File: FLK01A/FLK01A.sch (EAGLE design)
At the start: 31 parts, among them J1 M10SMD_MALE, J2 M10SMD_MALE, U1 LPC812TSSOP20, U2 EKMBTO5, U3 HTU21DSMD, U4 MMA8452Q, U5 VCNL4000, U6 MPL3115A2LGA8, U7 MMDT3904, Y1 12MHZ

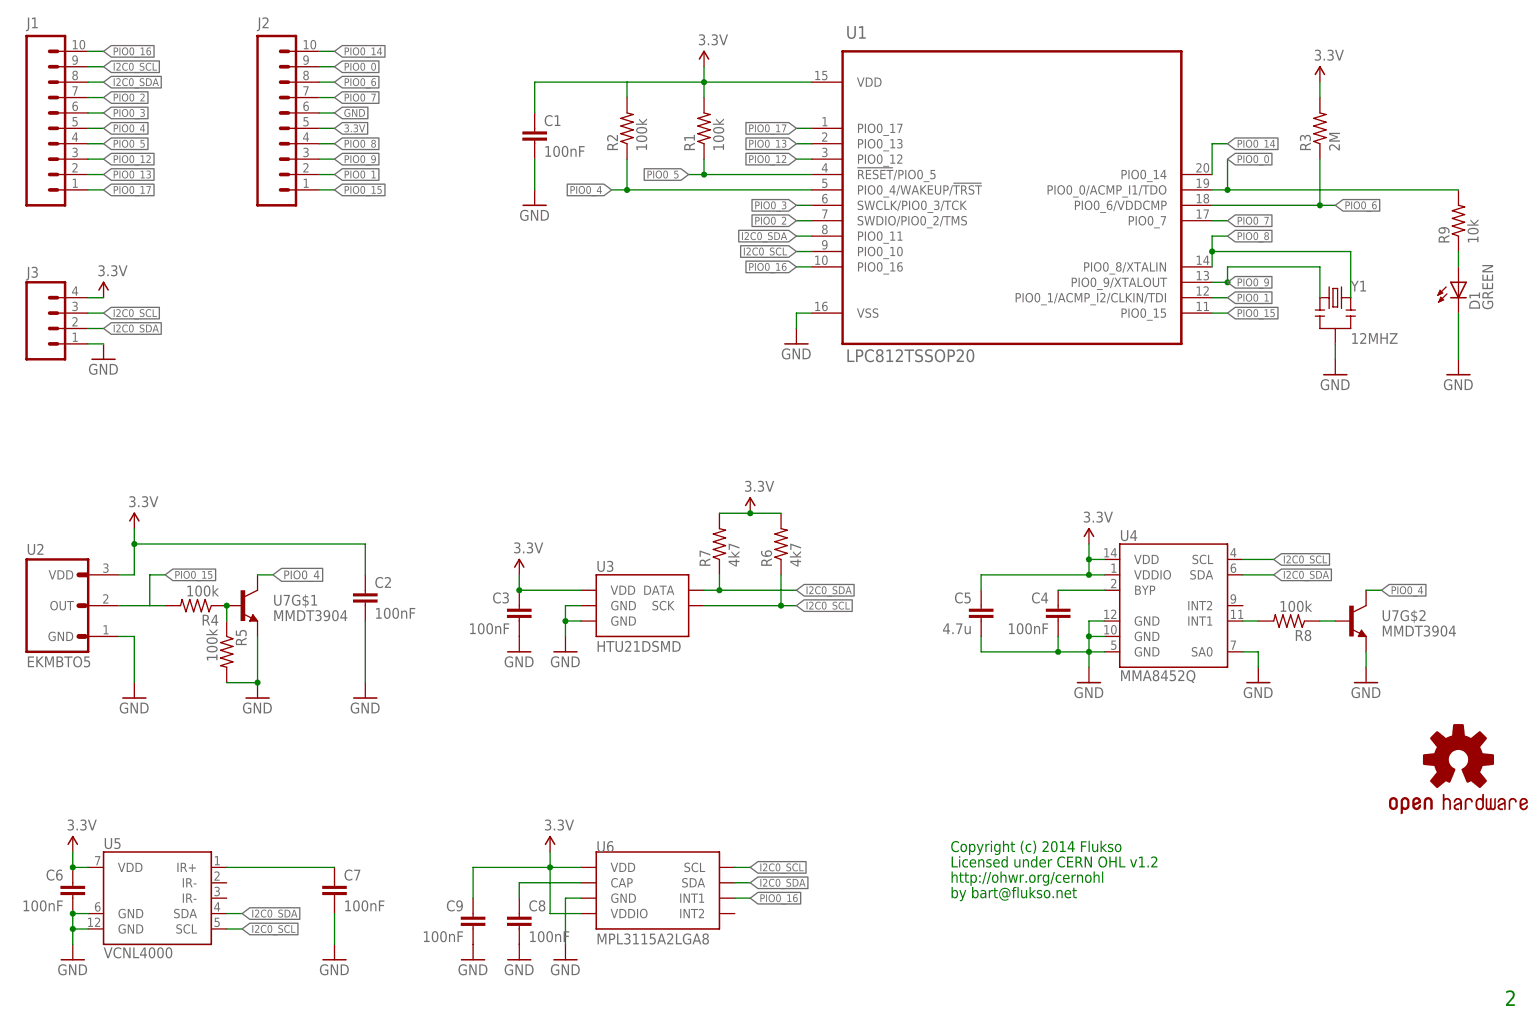
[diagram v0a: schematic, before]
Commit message: [pcb] clarify pin functions
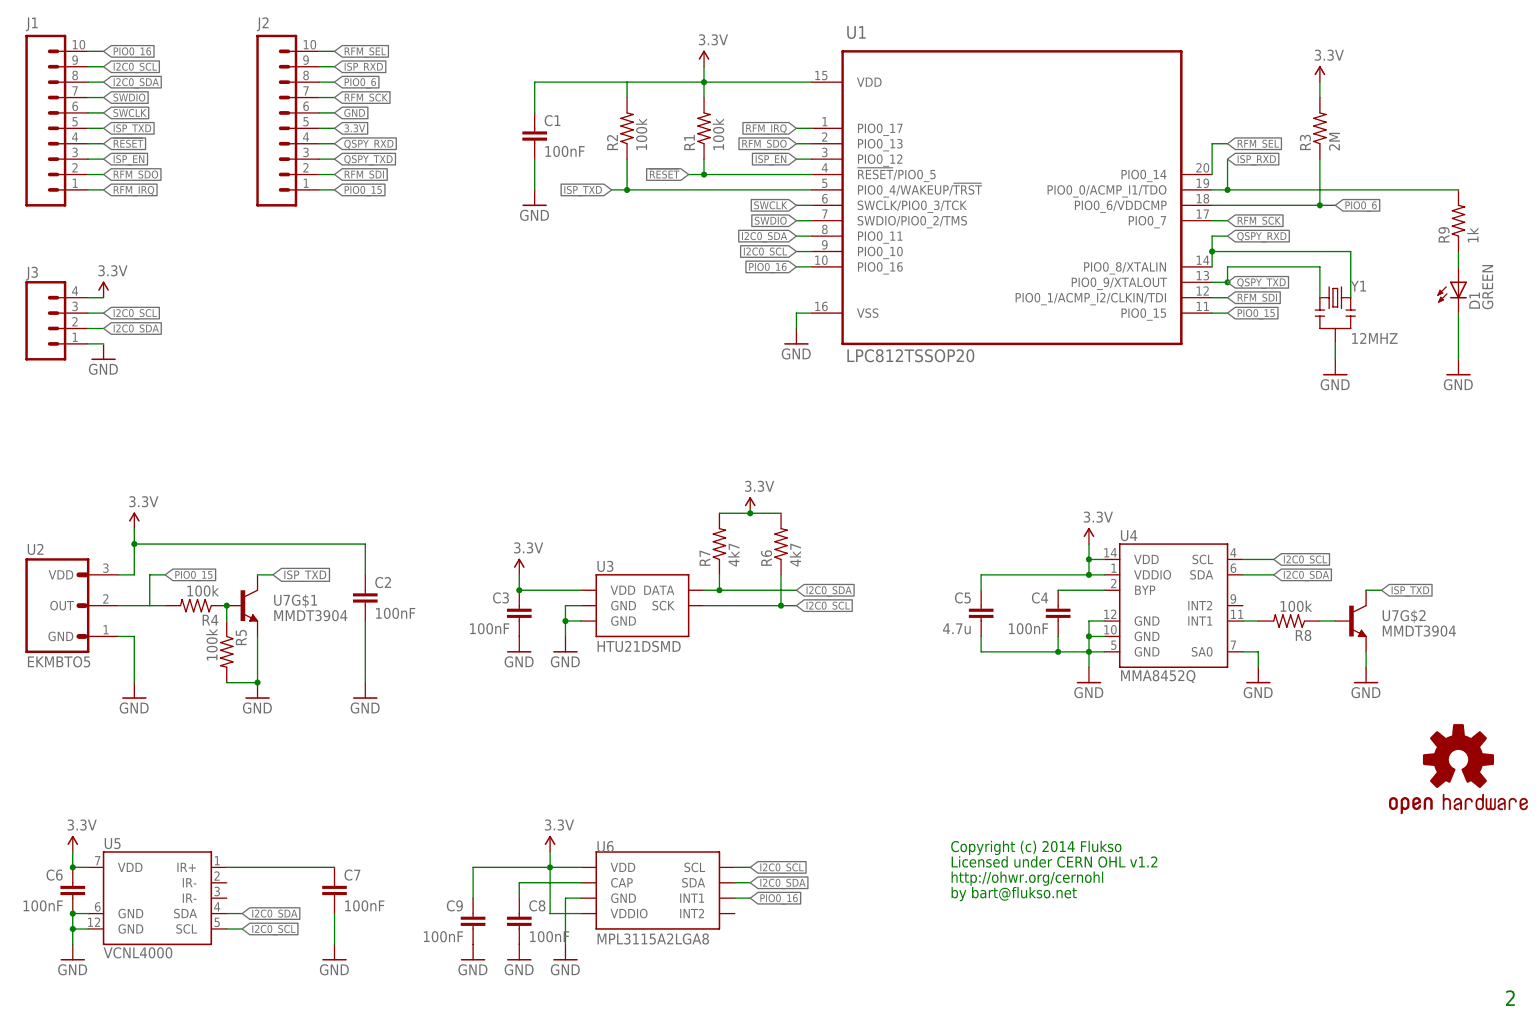
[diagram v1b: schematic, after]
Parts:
- R9: value 10k -> 1k
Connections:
- net PIO0_0 renamed ISP_RXD
- net PIO0_1 renamed RFM_SDI
- net PIO0_12 renamed !ISP_EN!
- net PIO0_13 renamed RFM_SDO
- net PIO0_14 renamed RFM_SEL
- net PIO0_17 renamed RFM_IRQ
- net PIO0_2 renamed SWDIO
- net PIO0_3 renamed SWCLK
- net PIO0_4 renamed ISP_TXD
- net PIO0_5 renamed !RESET!
- net PIO0_7 renamed RFM_SCK
- net PIO0_8 renamed QSPY_RXD
- net PIO0_9 renamed QSPY_TXD
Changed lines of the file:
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@@
 <part name="U3" library="flukso" deviceset="HTU21D" device="SMD"/>
 <part name="D1" library="SparkFun-LED" deviceset="LED-GREEN" device="0603" value="GREEN"/>
-<part name="R9" library="SparkFun-Passives" deviceset="RESISTOR" device="0402-RES" value="10k"/>
+<part name="R9" library="SparkFun-Passives" deviceset="RESISTOR" device="0402-RES" value="1k"/>
 <part name="GND17" library="SparkFun-Aesthetics" deviceset="GND" device=""/>
 <part name="J3" library="SparkFun-Connectors" deviceset="M04" device="1X04_NO_SILK"/>
@@
 </segment>
 </net>
-<net name="PIO0_17" class="0">
+<net name="RFM_IRQ" class="0">
 <segment>
 <pinref part="U1" gate="A" pin="PIO0_17"/>
@@
 </segment>
 </net>
-<net name="PIO0_13" class="0">
+<net name="RFM_SDO" class="0">
 <segment>
 <pinref part="U1" gate="A" pin="PIO0_13"/>
@@
 </segment>
 </net>
-<net name="PIO0_12" class="0">
+<net name="!ISP_EN!" class="0">
 <segment>
 <pinref part="U1" gate="A" pin="PIO0_12"/>
@@
 </segment>
 </net>
-<net name="PIO0_5" class="0">
+<net name="!RESET!" class="0">
 <segment>
 <pinref part="U1" gate="A" pin="!RESET!/PIO0_5"/>
@@
 </segment>
 </net>
-<net name="PIO0_4" class="0">
+<net name="ISP_TXD" class="0">
 <segment>
 <pinref part="U1" gate="A" pin="PIO0_4/WAKEUP/!TRST!"/>
@@
 </segment>
 </net>
-<net name="PIO0_3" class="0">
+<net name="SWCLK" class="0">
 <segment>
 <pinref part="U1" gate="A" pin="SWCLK/PIO0_3/TCK"/>
@@
 </segment>
 </net>
-<net name="PIO0_2" class="0">
+<net name="SWDIO" class="0">
 <segment>
 <pinref part="U1" gate="A" pin="SWDIO/PIO0_2/TMS"/>
@@
 </segment>
 </net>
-<net name="PIO0_14" class="0">
+<net name="RFM_SEL" class="0">
 <segment>
 <pinref part="U1" gate="A" pin="PIO0_14"/>
@@
 </segment>
 </net>
-<net name="PIO0_0" class="0">
+<net name="ISP_RXD" class="0">
 <segment>
 <pinref part="U1" gate="A" pin="PIO0_0/ACMP_I1/TDO"/>
@@
 </segment>
 </net>
-<net name="PIO0_7" class="0">
+<net name="RFM_SCK" class="0">
 <segment>
 <pinref part="U1" gate="A" pin="PIO0_7"/>
@@
 </segment>
 </net>
-<net name="PIO0_9" class="0">
+<net name="QSPY_TXD" class="0">
 <segment>
 <pinref part="U1" gate="A" pin="PIO0_9/XTALOUT"/>
@@
 </segment>
 </net>
-<net name="PIO0_1" class="0">
+<net name="RFM_SDI" class="0">
 <segment>
 <pinref part="U1" gate="A" pin="PIO0_1/ACMP_I2/CLKIN/TDI"/>
@@
 </segment>
 </net>
-<net name="PIO0_8" class="0">
+<net name="QSPY_RXD" class="0">
 <segment>
 <pinref part="U1" gate="A" pin="PIO0_8/XTALIN"/>

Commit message: [pcb] re-assign sensor interrupt pins
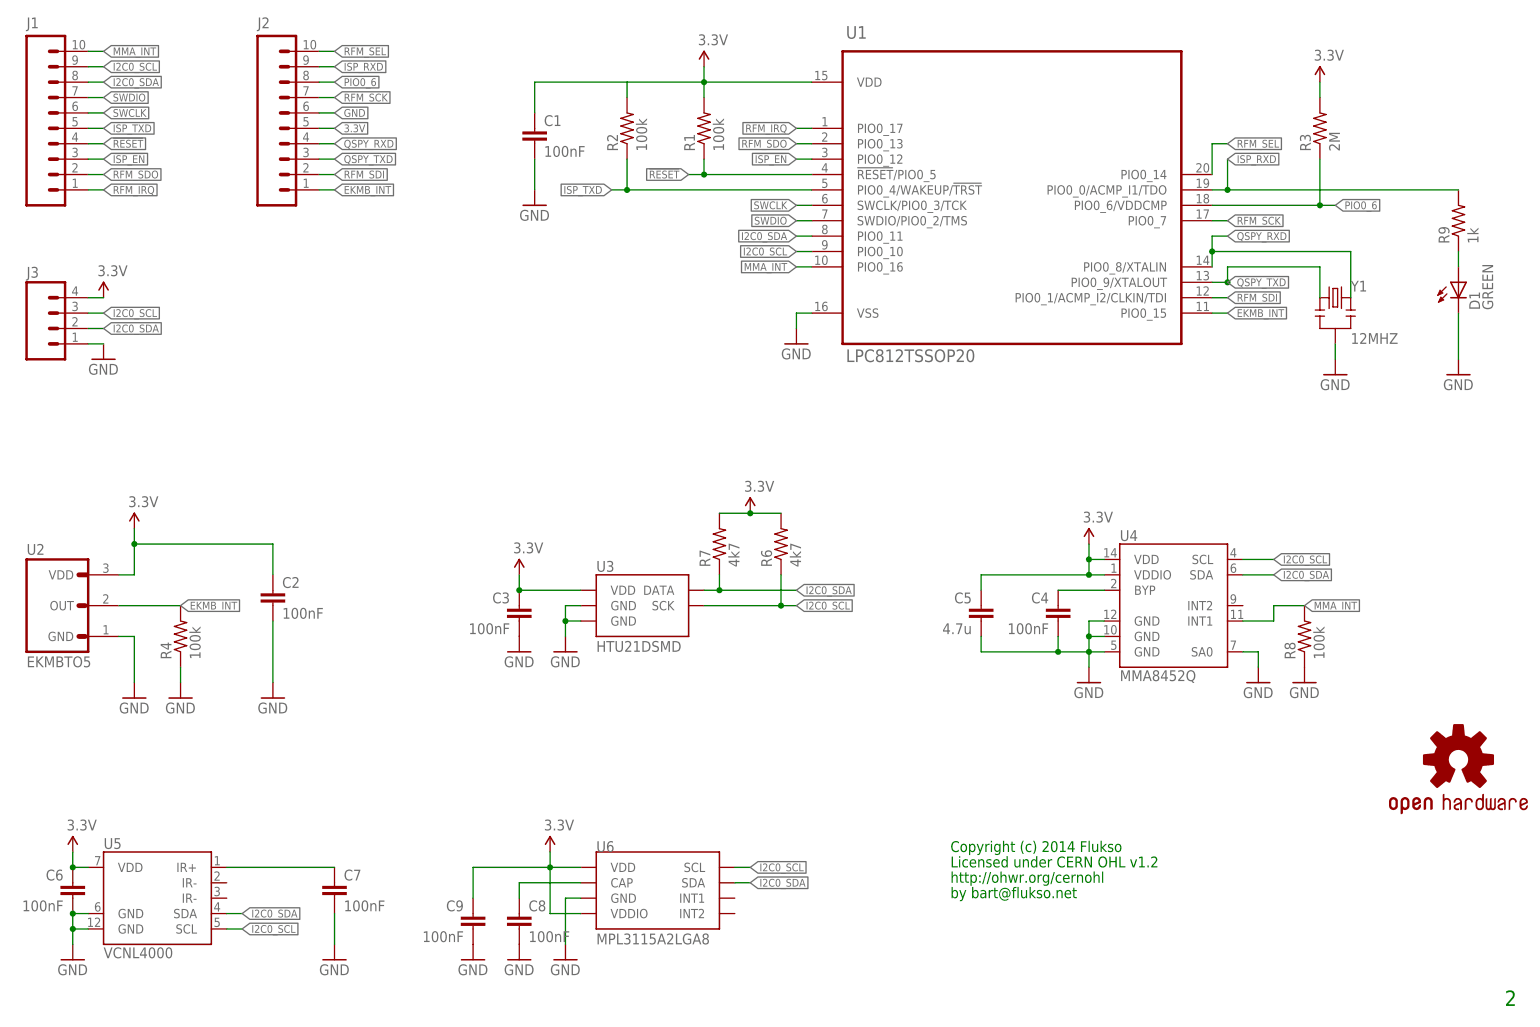
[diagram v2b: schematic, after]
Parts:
- removed R5: 100k, SparkFun-Passives:RESISTOR0402-RES
- removed U7: MMDT3904, SparkFun-DiscreteSemi:MMDT3904
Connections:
- net PIO0_15 renamed EKMB_INT
- removed net N$2: R4.1, R5.1, U7G$1.B
- removed net N$4: R8.2, U4.INT1
- removed net N$5: R8.1, U7G$2.B
- removed net PIO0_16: J1.10, U1.PIO0_16, U6.INT1
- new net MMA_INT: J1.10, R8.2, U1.PIO0_16, U4.INT1
- net GND: now also R4.1, R8.1; no longer R5.2, U7G$1.E, U7G$2.E
- net ISP_TXD: no longer U7G$1.C, U7G$2.C
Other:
- moved on the sheet: C2, R4, R8
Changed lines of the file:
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@@
 <part name="C5" library="flukso" deviceset="CAP" device="0603-CAP" value="4.7u"/>
 <part name="GND10" library="SparkFun-Aesthetics" deviceset="GND" device=""/>
-<part name="U7" library="SparkFun-DiscreteSemi" deviceset="MMDT3904" device=""/>
-<part name="R5" library="SparkFun-Passives" deviceset="RESISTOR" device="0402-RES" value="100k"/>
 <part name="R8" library="SparkFun-Passives" deviceset="RESISTOR" device="0402-RES" value="100k"/>
 <part name="GND11" library="SparkFun-Aesthetics" deviceset="GND" device=""/>
@@
 <instance part="GND4" gate="1" x="30.48" y="58.42"/>
 <instance part="SUPPLY3" gate="G$1" x="30.48" y="86.36"/>
-<instance part="C2" gate="G$1" x="68.58" y="73.66"/>
-<instance part="GND5" gate="1" x="68.58" y="58.42"/>
-<instance part="R4" gate="G$1" x="40.64" y="73.66" rot="R180"/>
-<instance part="GND6" gate="1" x="50.8" y="58.42"/>
+<instance part="C2" gate="G$1" x="53.34" y="73.66"/>
+<instance part="GND5" gate="1" x="53.34" y="58.42"/>
+<instance part="R4" gate="G$1" x="38.1" y="68.58" rot="R90"/>
+<instance part="GND6" gate="1" x="38.1" y="58.42"/>
 <instance part="GND7" gate="1" x="101.6" y="66.04"/>
 <instance part="SUPPLY4" gate="G$1" x="93.98" y="78.74"/>
@@
 <instance part="C5" gate="G$1" x="170.18" y="71.12" rot="MR0"/>
 <instance part="GND10" gate="1" x="215.9" y="60.96"/>
-<instance part="U7" gate="G$1" x="48.26" y="73.66"/>
-<instance part="U7" gate="G$2" x="231.14" y="71.12"/>
-<instance part="R5" gate="G$1" x="45.72" y="66.04" rot="R270"/>
-<instance part="R8" gate="G$1" x="220.98" y="71.12" rot="R180"/>
-<instance part="GND11" gate="1" x="233.68" y="60.96"/>
+<instance part="R8" gate="G$1" x="223.52" y="68.58" rot="R90"/>
+<instance part="GND11" gate="1" x="223.52" y="60.96"/>
 <instance part="U5" gate="G$1" x="33.02" y="25.4"/>
 <instance part="SUPPLY7" gate="G$1" x="20.32" y="33.02"/>
@@
 <pinref part="C2" gate="G$1" pin="2"/>
 <pinref part="GND5" gate="1" pin="GND"/>
-<wire x1="68.58" y1="71.12" x2="68.58" y2="60.96" width="0.1524" layer="91"/>
-</segment>
-<segment>
-<pinref part="GND6" gate="1" pin="GND"/>
-<wire x1="50.8" y1="68.58" x2="50.8" y2="60.96" width="0.1524" layer="91"/>
-<pinref part="U7" gate="G$1" pin="E"/>
-<pinref part="R5" gate="G$1" pin="2"/>
-<wire x1="45.72" y1="60.96" x2="50.8" y2="60.96" width="0.1524" layer="91"/>
-<junction x="50.8" y="60.96"/>
+<wire x1="53.34" y1="71.12" x2="53.34" y2="60.96" width="0.1524" layer="91"/>
 </segment>
 <segment>
@@
 </segment>
 <segment>
-<pinref part="U7" gate="G$2" pin="E"/>
-<pinref part="GND11" gate="1" pin="GND"/>
-<wire x1="233.68" y1="66.04" x2="233.68" y2="63.5" width="0.1524" layer="91"/>
-</segment>
-<segment>
 <pinref part="U5" gate="G$1" pin="GND@0"/>
 <pinref part="GND12" gate="1" pin="GND"/>
@@
 <pinref part="GND18" gate="1" pin="GND"/>
 </segment>
+<segment>
+<pinref part="R4" gate="G$1" pin="1"/>
+<pinref part="GND6" gate="1" pin="GND"/>
+<wire x1="38.1" y1="63.5" x2="38.1" y2="60.96" width="0.1524" layer="91"/>
+</segment>
+<segment>
+<pinref part="R8" gate="G$1" pin="1"/>
+<pinref part="GND11" gate="1" pin="GND"/>
+</segment>
 </net>
 <net name="RFM_IRQ" class="0">
@@
 <label x="25.4" y="152.4" size="1.27" layer="95" xref="yes"/>
 </segment>
-<segment>
-<wire x1="50.8" y1="78.74" x2="53.34" y2="78.74" width="0.1524" layer="91"/>
-<label x="53.34" y="78.74" size="1.4224" layer="95" xref="yes"/>
-<pinref part="U7" gate="G$1" pin="C"/>
-</segment>
-<segment>
-<pinref part="U7" gate="G$2" pin="C"/>
-<wire x1="233.68" y1="76.2" x2="236.22" y2="76.2" width="0.1524" layer="91"/>
-<label x="236.22" y="76.2" size="1.27" layer="95" xref="yes"/>
-</segment>
 </net>
 <net name="SWCLK" class="0">
@@
 </segment>
 </net>
-<net name="PIO0_16" class="0">
+<net name="MMA_INT" class="0">
 <segment>
 <pinref part="U1" gate="A" pin="PIO0_16"/>
@@
 </segment>
 <segment>
-<pinref part="U6" gate="G$1" pin="INT1"/>
-<wire x1="129.54" y1="25.4" x2="132.08" y2="25.4" width="0.1524" layer="91"/>
-<label x="132.08" y="25.4" size="1.27" layer="95" xref="yes"/>
+<pinref part="U4" gate="G$1" pin="INT1"/>
+<wire x1="213.36" y1="71.12" x2="218.44" y2="71.12" width="0.1524" layer="91"/>
+<wire x1="218.44" y1="71.12" x2="218.44" y2="73.66" width="0.1524" layer="91"/>
+<pinref part="R8" gate="G$1" pin="2"/>
+<wire x1="218.44" y1="73.66" x2="223.52" y2="73.66" width="0.1524" layer="91"/>
+<label x="223.52" y="73.66" size="1.27" layer="95" xref="yes"/>
 </segment>
 </net>
@@
 </segment>
 </net>
-<net name="PIO0_15" class="0">
+<net name="EKMB_INT" class="0">
 <segment>
 <pinref part="U1" gate="A" pin="PIO0_15"/>
@@
 <pinref part="U2" gate="A" pin="OUT"/>
 <pinref part="R4" gate="G$1" pin="2"/>
-<wire x1="35.56" y1="73.66" x2="33.02" y2="73.66" width="0.1524" layer="91"/>
-<wire x1="33.02" y1="73.66" x2="27.94" y2="73.66" width="0.1524" layer="91"/>
-<wire x1="33.02" y1="73.66" x2="33.02" y2="78.74" width="0.1524" layer="91"/>
-<wire x1="33.02" y1="78.74" x2="35.56" y2="78.74" width="0.1524" layer="91"/>
-<label x="35.56" y="78.74" size="1.27" layer="95" xref="yes"/>
+<wire x1="38.1" y1="73.66" x2="27.94" y2="73.66" width="0.1524" layer="91"/>
+<label x="38.1" y="73.66" size="1.27" layer="95" xref="yes"/>
 </segment>
 </net>
@@
 <wire x1="30.48" y1="83.82" x2="30.48" y2="86.36" width="0.1524" layer="91"/>
 <pinref part="C2" gate="G$1" pin="1"/>
-<wire x1="30.48" y1="83.82" x2="68.58" y2="83.82" width="0.1524" layer="91"/>
-<wire x1="68.58" y1="83.82" x2="68.58" y2="78.74" width="0.1524" layer="91"/>
+<wire x1="30.48" y1="83.82" x2="53.34" y2="83.82" width="0.1524" layer="91"/>
+<wire x1="53.34" y1="83.82" x2="53.34" y2="78.74" width="0.1524" layer="91"/>
 <junction x="30.48" y="83.82"/>
 </segment>
@@
 </segment>
 </net>
-<net name="N$2" class="0">
-<segment>
-<pinref part="R4" gate="G$1" pin="1"/>
-<pinref part="U7" gate="G$1" pin="B"/>
-<pinref part="R5" gate="G$1" pin="1"/>
-<pinref part="R5" gate="G$1" pin="1"/>
-<wire x1="45.72" y1="71.12" x2="45.72" y2="73.66" width="0.1524" layer="91"/>
-<junction x="45.72" y="73.66"/>
-</segment>
-</net>
-<net name="N$4" class="0">
-<segment>
-<pinref part="U4" gate="G$1" pin="INT1"/>
-<pinref part="R8" gate="G$1" pin="2"/>
-<wire x1="213.36" y1="71.12" x2="215.9" y2="71.12" width="0.1524" layer="91"/>
-</segment>
-</net>
-<net name="N$5" class="0">
-<segment>
-<pinref part="R8" gate="G$1" pin="1"/>
-<pinref part="U7" gate="G$2" pin="B"/>
-<wire x1="226.06" y1="71.12" x2="228.6" y2="71.12" width="0.1524" layer="91"/>
-</segment>
-</net>

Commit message: [pcb] increase C5 size from 0603 to 0805
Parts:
- C5: value 4.7u -> 4.7uF; device flukso:CAP0603-CAP -> flukso:CAP0805
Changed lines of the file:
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@@
 <layer number="122" name="_bsilk" color="7" fill="1" visible="yes" active="yes"/>
 <layer number="125" name="_tNames" color="7" fill="1" visible="no" active="yes"/>
+<layer number="131" name="prix" color="7" fill="1" visible="yes" active="yes"/>
+<layer number="132" name="test" color="7" fill="1" visible="yes" active="yes"/>
 <layer number="144" name="Drill_legend" color="7" fill="1" visible="no" active="yes"/>
 <layer number="151" name="HeatSink" color="7" fill="1" visible="yes" active="yes"/>
@@
 <part name="GND9" library="SparkFun-Aesthetics" deviceset="GND" device=""/>
 <part name="C4" library="flukso" deviceset="CAP" device="0402-CAP" value="100nF"/>
-<part name="C5" library="flukso" deviceset="CAP" device="0603-CAP" value="4.7u"/>
 <part name="GND10" library="SparkFun-Aesthetics" deviceset="GND" device=""/>
 <part name="R8" library="SparkFun-Passives" deviceset="RESISTOR" device="0402-RES" value="100k"/>
@@
 <part name="GND18" library="SparkFun-Aesthetics" deviceset="GND" device=""/>
 <part name="SUPPLY9" library="SparkFun-Aesthetics" deviceset="3.3V" device=""/>
+<part name="C5" library="flukso" deviceset="CAP" device="0805" value="4.7uF"/>
 </parts>
 <sheets>
@@
 <instance part="GND9" gate="1" x="187.96" y="60.96"/>
 <instance part="C4" gate="G$1" x="182.88" y="71.12" rot="MR0"/>
-<instance part="C5" gate="G$1" x="170.18" y="71.12" rot="MR0"/>
 <instance part="GND10" gate="1" x="215.9" y="60.96"/>
 <instance part="R8" gate="G$1" x="223.52" y="68.58" rot="R90"/>
@@
 <instance part="GND18" gate="1" x="25.4" y="114.3"/>
 <instance part="SUPPLY9" gate="G$1" x="25.4" y="124.46"/>
+<instance part="C5" gate="G$1" x="170.18" y="71.12" rot="MR0"/>
 </instances>
 <busses>
@@
 <wire x1="182.88" y1="68.58" x2="182.88" y2="66.04" width="0.1524" layer="91"/>
 <wire x1="182.88" y1="66.04" x2="187.96" y2="66.04" width="0.1524" layer="91"/>
-<pinref part="C5" gate="G$1" pin="2"/>
 <wire x1="170.18" y1="68.58" x2="170.18" y2="66.04" width="0.1524" layer="91"/>
 <wire x1="170.18" y1="66.04" x2="182.88" y2="66.04" width="0.1524" layer="91"/>
 <junction x="182.88" y="66.04"/>
+<pinref part="C5" gate="G$1" pin="2"/>
 </segment>
 <segment>
@@
 <wire x1="187.96" y1="78.74" x2="187.96" y2="81.28" width="0.1524" layer="91"/>
 <junction x="187.96" y="81.28"/>
-<pinref part="C5" gate="G$1" pin="1"/>
 <wire x1="187.96" y1="78.74" x2="170.18" y2="78.74" width="0.1524" layer="91"/>
 <wire x1="170.18" y1="78.74" x2="170.18" y2="76.2" width="0.1524" layer="91"/>
 <junction x="187.96" y="78.74"/>
-</segment>
-<segment>
+<pinref part="C5" gate="G$1" pin="1"/>
+</segment>
+<segment>
